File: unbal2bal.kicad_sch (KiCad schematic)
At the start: 30 parts, among them J1 901, J2 NMJ6HFD2, J3 Mini-DIN-3, J4 Mini-DIN-4, U1 LM4562

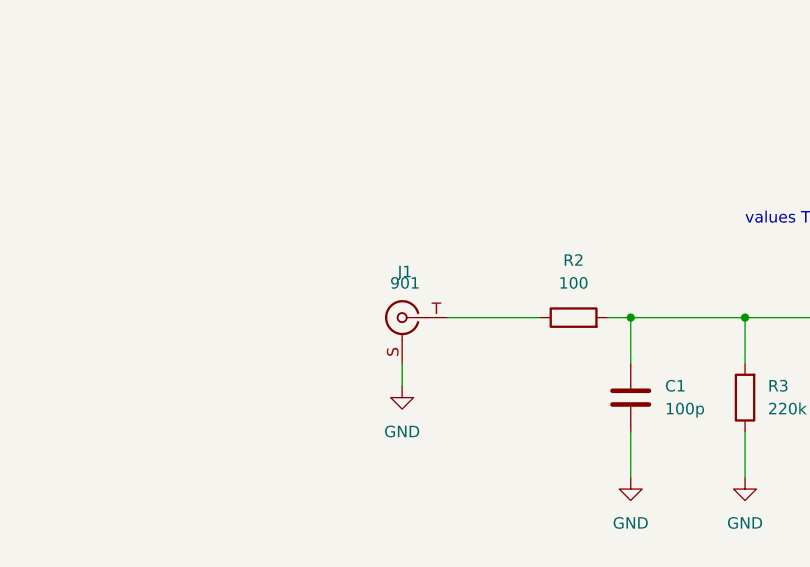
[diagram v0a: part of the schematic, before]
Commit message: switch RCA jack to a nicer model
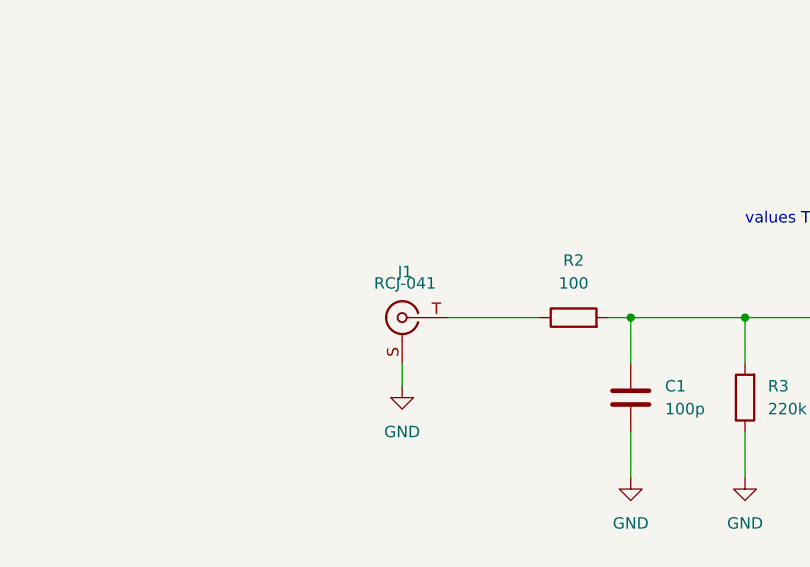
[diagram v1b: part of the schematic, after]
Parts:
- J1: value 901 -> RCJ-041; footprint Connector_Audio_gkeeth:RCA_Keystone_901_Horizontal -> Connector_Audio_gkeeth:RCA_CUI_RCJ-04x_Horizontal; Distributor PN 36-901-ND -> CP-1418-ND; Manufacturer Keystone -> CUI; Manufacturer PN 901 -> RCJ-041
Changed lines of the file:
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@@
     (in_bom yes) (on_board yes) (fields_autoplaced)
     (property "Reference" "J1" (id 0) (at 100.6474 107.95 0))
-    (property "Value" "901" (id 1) (at 100.6474 109.22 0)
+    (property "Value" "RCJ-041" (id 1) (at 100.6474 109.22 0)
       (effects (font (size 0 0)))
     )
-    (property "Footprint" "Connector_Audio_gkeeth:RCA_Keystone_901_Horizontal" (id 2) (at 100.33 113.03 0)
+    (property "Footprint" "Connector_Audio_gkeeth:RCA_CUI_RCJ-04x_Horizontal" (id 2) (at 100.33 113.03 0)
       (effects (font (size 1.27 1.27)) hide)
     )
@@
       (effects (font (size 1.27 1.27)) hide)
     )
-    (property "Manufacturer" "Keystone" (id 4) (at 100.33 113.03 0)
-      (effects (font (size 1.27 1.27)) hide)
-    )
-    (property "Manufacturer PN" "901" (id 5) (at 100.33 113.03 0)
+    (property "Manufacturer" "CUI" (id 4) (at 100.33 113.03 0)
+      (effects (font (size 1.27 1.27)) hide)
+    )
+    (property "Manufacturer PN" "RCJ-041" (id 5) (at 100.33 113.03 0)
       (effects (font (size 1.27 1.27)) hide)
     )
@@
       (effects (font (size 1.27 1.27)) hide)
     )
-    (property "Distributor PN" "36-901-ND" (id 7) (at 100.33 113.03 0)
+    (property "Distributor PN" "CP-1418-ND" (id 7) (at 100.33 113.03 0)
       (effects (font (size 1.27 1.27)) hide)
     )
@@
     )
     (path "/e70b34b3-715d-488a-9afc-d08a974cea76"
-      (reference "J1") (unit 1) (value "901") (footprint "Connector_Audio_gkeeth:RCA_Keystone_901_Horizontal")
+      (reference "J1") (unit 1) (value "RCJ-041") (footprint "Connector_Audio_gkeeth:RCA_CUI_RCJ-04x_Horizontal")
     )
     (path "/6b4bf41a-f92b-45af-85d0-8c22db24b04b"

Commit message: move output coupling caps to horizontal to fit into enclosure
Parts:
- C7, C8: footprint Capacitor_THT:C_Radial_D12.5mm_H25.0mm_P5.00mm -> Capacitor_THT_gkeeth:C_Radial_D12.5mm_H20.0mm_P5.00mm_Horizontal
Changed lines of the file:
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@@
   (title_block
     (title "Unbalanced to Balanced Audio Converter")
-    (date "2022-06-11")
-    (rev "0")
+    (date "${DATE}")
+    (rev "${VERSION}")
     (company "G. Keeth")
+    (comment 1 "${URL}")
     (comment 3 "fits Adafruit 2230 enclosure")
   )
@@
     (property "Reference" "C7" (id 0) (at 266.7 69.85 90))
     (property "Value" "220u" (id 1) (at 266.7 72.39 90))
-    (property "Footprint" "Capacitor_THT:C_Radial_D12.5mm_H25.0mm_P5.00mm" (id 2) (at 270.51 76.5048 0)
+    (property "Footprint" "Capacitor_THT_gkeeth:C_Radial_D12.5mm_H20.0mm_P5.00mm_Horizontal" (id 2) (at 270.51 76.5048 0)
       (effects (font (size 1.27 1.27)) hide)
     )
@@
     (property "Reference" "C8" (id 0) (at 266.7 119.38 90))
     (property "Value" "220u" (id 1) (at 266.7 121.92 90))
-    (property "Footprint" "Capacitor_THT:C_Radial_D12.5mm_H25.0mm_P5.00mm" (id 2) (at 270.51 126.0348 0)
+    (property "Footprint" "Capacitor_THT_gkeeth:C_Radial_D12.5mm_H20.0mm_P5.00mm_Horizontal" (id 2) (at 270.51 126.0348 0)
       (effects (font (size 1.27 1.27)) hide)
     )
@@
     )
     (path "/35496eef-8204-4ddc-9f1a-bc2d69ec9952"
-      (reference "C7") (unit 1) (value "220u") (footprint "Capacitor_THT:C_Radial_D12.5mm_H25.0mm_P5.00mm")
+      (reference "C7") (unit 1) (value "220u") (footprint "Capacitor_THT_gkeeth:C_Radial_D12.5mm_H20.0mm_P5.00mm_Horizontal")
     )
     (path "/c580afc4-5a6f-448f-9b88-86107feccdc1"
-      (reference "C8") (unit 1) (value "220u") (footprint "Capacitor_THT:C_Radial_D12.5mm_H25.0mm_P5.00mm")
+      (reference "C8") (unit 1) (value "220u") (footprint "Capacitor_THT_gkeeth:C_Radial_D12.5mm_H20.0mm_P5.00mm_Horizontal")
     )
     (path "/f91439e2-323e-4ecd-a6ad-92a4549f1cba"

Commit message: minor updates, labels, etc
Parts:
- added TP1, TP2: TestPoint_2Pole, Connector_PinHeader_2.54mm:PinHeader_1x02_P2.54mm_Vertical, symbol Connector:TestPoint_2Pole
- J3: Distributor (none) -> Digikey; Distributor PN (none) -> 2092-KMDGX-3S-BS-ND; Manufacturer (none) -> Kycon; Manufacturer PN (none) -> KMDGX-3S-BS
- J4: Distributor (none) -> Digikey; Distributor PN (none) -> 2092-KMDGX-4S-BS-ND; Manufacturer (none) -> Kycon; Manufacturer PN (none) -> KMDGX-4S-BS
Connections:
- net GND: now also TP1.1, TP2.1
- net VCC: now also TP1.2
- net VEE: now also TP2.2
- net hot_out: now reaches C7.2, J2.T, J2.TN, R11.2
- net unbal_in: now reaches J1.T, R2.1
- net cold_out: now reaches C8.2, J2.R, J2.RN, R12.2
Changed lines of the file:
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@@
+    (stroke (width 0) (type default) (color 0 0 0 0))
+  )
+  (wire (pts (xy 146.05 237.49) (xy 146.05 236.22))
     (stroke (width 0) (type default) (color 0 0 0 0))
   )
@@
     (stroke (width 0) (type default) (color 0 0 0 0))
   )
+  (wire (pts (xy 166.37 220.98) (xy 166.37 219.71))
+    (stroke (width 0) (type default) (color 0 0 0 0))
+  )
   (wire (pts (xy 83.82 238.76) (xy 80.01 238.76))
     (stroke (width 0) (type default) (color 0 0 0 0))
@@
     (stroke (width 0) (type default) (color 0 0 0 0))
   )
+  (wire (pts (xy 146.05 220.98) (xy 151.13 220.98))
+    (stroke (width 0) (type default) (color 0 0 0 0))
+  )
   (wire (pts (xy 33.02 212.09) (xy 33.02 217.17))
     (stroke (width 0) (type default) (color 0 0 0 0))
@@
     (stroke (width 0) (type default) (color 0 0 0 0))
   )
+  (wire (pts (xy 146.05 236.22) (xy 151.13 236.22))
+    (stroke (width 0) (type default) (color 0 0 0 0))
+  )
   (wire (pts (xy 80.01 241.3) (xy 83.82 241.3))
     (stroke (width 0) (type default) (color 0 0 0 0))
@@
     (stroke (width 0) (type default) (color 0 0 0 0))
   )
+  (wire (pts (xy 161.29 220.98) (xy 166.37 220.98))
+    (stroke (width 0) (type default) (color 0 0 0 0))
+  )
   (wire (pts (xy 163.83 125.73) (xy 163.83 130.81))
     (stroke (width 0) (type default) (color 0 0 0 0))
@@
     (stroke (width 0) (type default) (color 0 0 0 0))
   )
+  (wire (pts (xy 166.37 236.22) (xy 166.37 237.49))
+    (stroke (width 0) (type default) (color 0 0 0 0))
+  )
   (wire (pts (xy 82.55 199.39) (xy 82.55 196.85))
     (stroke (width 0) (type default) (color 0 0 0 0))
@@
     (stroke (width 0) (type default) (color 0 0 0 0))
   )
+  (wire (pts (xy 161.29 236.22) (xy 166.37 236.22))
+    (stroke (width 0) (type default) (color 0 0 0 0))
+  )
   (wire (pts (xy 93.98 204.47) (xy 93.98 205.74))
     (stroke (width 0) (type default) (color 0 0 0 0))
@@
   )
   (wire (pts (xy 209.55 110.49) (xy 212.09 110.49))
+    (stroke (width 0) (type default) (color 0 0 0 0))
+  )
+  (wire (pts (xy 146.05 222.25) (xy 146.05 220.98))
     (stroke (width 0) (type default) (color 0 0 0 0))
   )
@@
   (text "Populate if gain is needed" (at 175.26 128.27 0)
     (effects (font (size 1.27 1.27)) (justify left bottom))
+  )
+  (label "hot_out" (at 311.15 77.47 0)
+    (effects (font (size 1.27 1.27)) (justify left bottom))
+  )
+  (label "unbal_in" (at 106.68 113.03 0)
+    (effects (font (size 1.27 1.27)) (justify left bottom))
+  )
+  (label "cold_out" (at 311.15 85.09 0)
+    (effects (font (size 1.27 1.27)) (justify left bottom))
+  )
+  (symbol (lib_id "Connector:TestPoint_2Pole") (at 156.21 220.98 0) (unit 1)
+    (in_bom yes) (on_board yes) (fields_autoplaced)
+    (property "Reference" "TP1" (id 0) (at 156.21 214.63 0))
+    (property "Value" "TestPoint_2Pole" (id 1) (at 156.21 217.17 0))
+    (property "Footprint" "Connector_PinHeader_2.54mm:PinHeader_1x02_P2.54mm_Vertical" (id 2) (at 156.21 220.98 0)
+      (effects (font (size 1.27 1.27)) hide)
+    )
+    (property "Datasheet" "~" (id 3) (at 156.21 220.98 0)
+      (effects (font (size 1.27 1.27)) hide)
+    )
+    (pin "1")
+    (pin "2")
   )
   (symbol (lib_id "Device:C") (at 151.13 113.03 90) (unit 1)
@@
     (pin "2")
   )
+  (symbol (lib_id "power:VEE") (at 166.37 237.49 180) (unit 1)
+    (in_bom yes) (on_board yes) (fields_autoplaced)
+    (property "Reference" "#PWR?" (id 0) (at 166.37 233.68 0)
+      (effects (font (size 1.27 1.27)) hide)
+    )
+    (property "Value" "VEE" (id 1) (at 166.37 242.57 0))
+    (property "Footprint" "" (id 2) (at 166.37 237.49 0)
+      (effects (font (size 1.27 1.27)) hide)
+    )
+    (property "Datasheet" "" (id 3) (at 166.37 237.49 0)
+      (effects (font (size 1.27 1.27)) hide)
+    )
+    (pin "1")
+  )
   (symbol (lib_id "power:GND") (at 26.67 213.36 0) (unit 1)
     (in_bom yes) (on_board yes) (fields_autoplaced)
@@
     (pin "2")
   )
+  (symbol (lib_id "power:GND") (at 146.05 222.25 0) (unit 1)
+    (in_bom yes) (on_board yes) (fields_autoplaced)
+    (property "Reference" "#PWR?" (id 0) (at 146.05 228.6 0)
+      (effects (font (size 1.27 1.27)) hide)
+    )
+    (property "Value" "GND" (id 1) (at 146.05 227.33 0))
+    (property "Footprint" "" (id 2) (at 146.05 222.25 0)
+      (effects (font (size 1.27 1.27)) hide)
+    )
+    (property "Datasheet" "" (id 3) (at 146.05 222.25 0)
+      (effects (font (size 1.27 1.27)) hide)
+    )
+    (pin "1")
+  )
   (symbol (lib_id "Device:LED") (at 33.02 220.98 90) (unit 1)
     (in_bom yes) (on_board yes) (fields_autoplaced)
@@
       (effects (font (size 1.27 1.27)) hide)
     )
+    (property "Manufacturer" "Kycon" (id 4) (at 91.44 241.3 0)
+      (effects (font (size 1.27 1.27)) hide)
+    )
+    (property "Manufacturer PN" "KMDGX-4S-BS" (id 5) (at 91.44 241.3 0)
+      (effects (font (size 1.27 1.27)) hide)
+    )
+    (property "Distributor" "Digikey" (id 6) (at 91.44 241.3 0)
+      (effects (font (size 1.27 1.27)) hide)
+    )
+    (property "Distributor PN" "2092-KMDGX-4S-BS-ND" (id 7) (at 91.44 241.3 0)
+      (effects (font (size 1.27 1.27)) hide)
+    )
     (pin "1")
     (pin "2")
@@
     (pin "1")
     (pin "2")
+  )
+  (symbol (lib_id "power:GND") (at 146.05 237.49 0) (unit 1)
+    (in_bom yes) (on_board yes) (fields_autoplaced)
+    (property "Reference" "#PWR?" (id 0) (at 146.05 243.84 0)
+      (effects (font (size 1.27 1.27)) hide)
+    )
+    (property "Value" "GND" (id 1) (at 146.05 242.57 0))
+    (property "Footprint" "" (id 2) (at 146.05 237.49 0)
+      (effects (font (size 1.27 1.27)) hide)
+    )
+    (property "Datasheet" "" (id 3) (at 146.05 237.49 0)
+      (effects (font (size 1.27 1.27)) hide)
+    )
+    (pin "1")
   )
   (symbol (lib_id "power:VEE") (at 33.02 243.84 180) (unit 1)
@@
     (pin "1")
   )
+  (symbol (lib_id "Connector:TestPoint_2Pole") (at 156.21 236.22 0) (unit 1)
+    (in_bom yes) (on_board yes) (fields_autoplaced)
+    (property "Reference" "TP2" (id 0) (at 156.21 229.87 0))
+    (property "Value" "TestPoint_2Pole" (id 1) (at 156.21 232.41 0))
+    (property "Footprint" "Connector_PinHeader_2.54mm:PinHeader_1x02_P2.54mm_Vertical" (id 2) (at 156.21 236.22 0)
+      (effects (font (size 1.27 1.27)) hide)
+    )
+    (property "Datasheet" "~" (id 3) (at 156.21 236.22 0)
+      (effects (font (size 1.27 1.27)) hide)
+    )
+    (pin "1")
+    (pin "2")
+  )
   (symbol (lib_id "Amplifier_Operational:LM4562") (at 187.96 110.49 0) (mirror x) (unit 1)
     (in_bom yes) (on_board yes) (fields_autoplaced)
@@
     (pin "1")
   )
+  (symbol (lib_id "power:VCC") (at 166.37 219.71 0) (unit 1)
+    (in_bom yes) (on_board yes) (fields_autoplaced)
+    (property "Reference" "#PWR?" (id 0) (at 166.37 223.52 0)
+      (effects (font (size 1.27 1.27)) hide)
+    )
+    (property "Value" "VCC" (id 1) (at 166.37 214.63 0))
+    (property "Footprint" "" (id 2) (at 166.37 219.71 0)
+      (effects (font (size 1.27 1.27)) hide)
+    )
+    (property "Datasheet" "" (id 3) (at 166.37 219.71 0)
+      (effects (font (size 1.27 1.27)) hide)
+    )
+    (pin "1")
+  )
   (symbol (lib_id "Device:R") (at 189.23 77.47 270) (unit 1)
     (in_bom yes) (on_board yes) (fields_autoplaced)
@@
     )
     (property "Datasheet" "http://www.assmann-wsw.com/fileadmin/catalogue/10_MiniDIN_rev4-0.pdf" (id 3) (at 93.98 196.85 0)
+      (effects (font (size 1.27 1.27)) hide)
+    )
+    (property "Manufacturer" "Kycon" (id 4) (at 93.98 196.85 0)
+      (effects (font (size 1.27 1.27)) hide)
+    )
+    (property "Manufacturer PN" "KMDGX-3S-BS" (id 5) (at 93.98 196.85 0)
+      (effects (font (size 1.27 1.27)) hide)
+    )
+    (property "Distributor" "Digikey" (id 6) (at 93.98 196.85 0)
+      (effects (font (size 1.27 1.27)) hide)
+    )
+    (property "Distributor PN" "2092-KMDGX-3S-BS-ND" (id 7) (at 93.98 196.85 0)
       (effects (font (size 1.27 1.27)) hide)
     )
@@
       (reference "#PWR0103") (unit 1) (value "VEE") (footprint "")
     )
+    (path "/0bba2cce-ada1-46e9-89f1-3d95583a37aa"
+      (reference "#PWR?") (unit 1) (value "VEE") (footprint "")
+    )
+    (path "/354d4dd3-f85a-4de8-9ef1-52f23b9df446"
+      (reference "#PWR?") (unit 1) (value "GND") (footprint "")
+    )
+    (path "/67301ee6-9f3f-4a48-a67f-000f870c9eb0"
+      (reference "#PWR?") (unit 1) (value "GND") (footprint "")
+    )
+    (path "/a38e303e-e931-4f5f-a2c2-7b8c9c006565"
+      (reference "#PWR?") (unit 1) (value "VCC") (footprint "")
+    )
     (path "/902fcc74-b504-4773-8dd9-b41734074b50"
       (reference "C1") (unit 1) (value "100p") (footprint "Capacitor_SMD:C_0805_2012Metric")
@@
       (reference "R12") (unit 1) (value "47k") (footprint "Resistor_SMD:R_1206_3216Metric")
     )
+    (path "/08382fbd-76b8-4265-a1e2-9d4156912e55"
+      (reference "TP1") (unit 1) (value "TestPoint_2Pole") (footprint "Connector_PinHeader_2.54mm:PinHeader_1x02_P2.54mm_Vertical")
+    )
+    (path "/72e56f26-c9d1-4a21-84a8-941067bca59e"
+      (reference "TP2") (unit 1) (value "TestPoint_2Pole") (footprint "Connector_PinHeader_2.54mm:PinHeader_1x02_P2.54mm_Vertical")
+    )
     (path "/74b9f962-6894-4e19-8ef5-db26705c61a1"

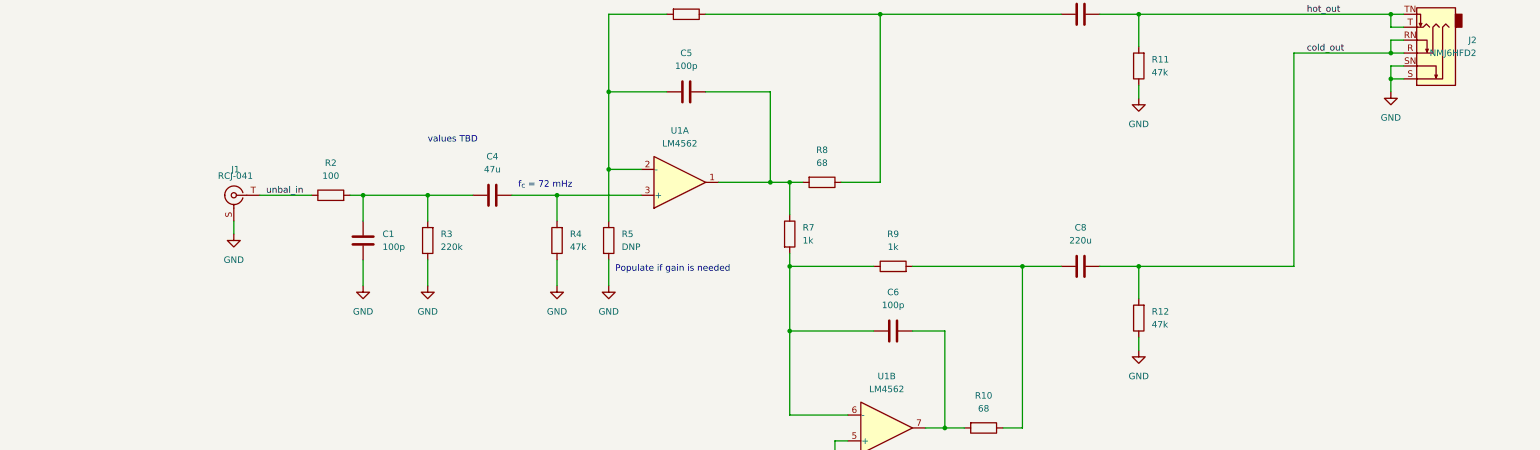
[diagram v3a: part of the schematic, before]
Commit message: update grounding
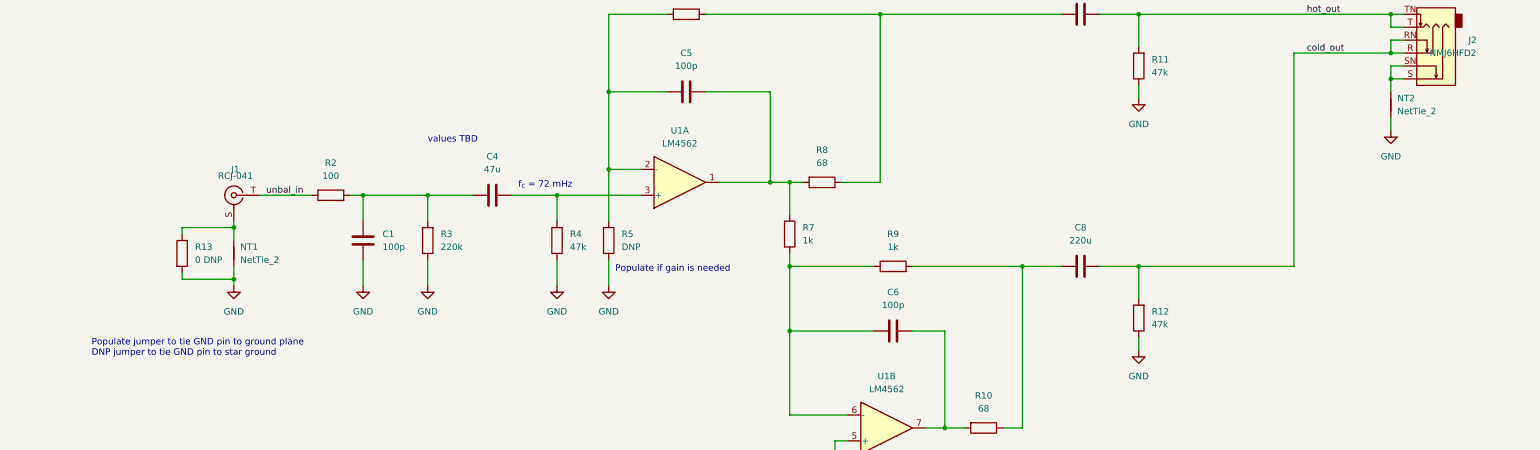
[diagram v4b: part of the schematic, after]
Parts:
- added NT1, NT2: NetTie_2, Net_Tie_gkeeth:NetTie-2_SMD_Pad1.0mm, symbol Device:NetTie_2
- added R13: 0 DNP, Resistor_SMD:R_1206_3216Metric, symbol Device:R
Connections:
- net GND: now also NT1.1, NT2.2, R13.2; no longer J1.S, J2.S, J2.SN
- new net: J1.S, NT1.2, R13.1
- new net: J2.S, J2.SN, NT2.1
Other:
- note added: "Populate jumper to tie GND pin to ground plane DNP jumper to tie GND pin to star ground"

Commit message: update part numbers
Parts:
- C2, C3: Distributor (none) -> Digikey; Distributor PN (none) -> 493-1081-ND; Manufacturer (none) -> Nichicon; Manufacturer PN (none) -> UVR1V101MED; Voltage Rating 25V -> 35V
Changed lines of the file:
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@@
       (effects (font (size 1.27 1.27)) hide)
     )
-    (property "Voltage Rating" "25V" (id 5) (at 130.81 200.66 0)
+    (property "Voltage Rating" "35V" (id 5) (at 130.81 200.66 0)
+      (effects (font (size 1.27 1.27)) hide)
+    )
+    (property "Distributor" "Digikey" (id 6) (at 130.81 200.66 0)
+      (effects (font (size 1.27 1.27)) hide)
+    )
+    (property "Distributor PN" "493-1081-ND" (id 7) (at 130.81 200.66 0)
+      (effects (font (size 1.27 1.27)) hide)
+    )
+    (property "Manufacturer" "Nichicon" (id 8) (at 130.81 200.66 0)
+      (effects (font (size 1.27 1.27)) hide)
+    )
+    (property "Manufacturer PN" "UVR1V101MED" (id 9) (at 130.81 200.66 0)
       (effects (font (size 1.27 1.27)) hide)
     )
@@
       (effects (font (size 1.27 1.27)) hide)
     )
-    (property "Voltage Rating" "25V" (id 9) (at 130.81 189.23 0)
-      (effects (font (size 1.27 1.27)) hide)
-    )
+    (property "Voltage Rating" "35V" (id 9) (at 130.81 189.23 0)
+      (effects (font (size 1.27 1.27)) hide)
+    )
+    (property "Distributor" "Digikey" (id 10) (at 130.81 189.23 0)
+      (effects (font (size 1.27 1.27)) hide)
+    )
+    (property "Distributor PN" "493-1081-ND" (id 11) (at 130.81 189.23 0)
+      (effects (font (size 1.27 1.27)) hide)
+    )
+    (property "Manufacturer" "Nichicon" (id 12) (at 130.81 189.23 0)
+      (effects (font (size 1.27 1.27)) hide)
+    )
+    (property "Manufacturer PN" "UVR1V101MED" (id 13) (at 130.81 189.23 0)
+      (effects (font (size 1.27 1.27)) hide)
+    )
